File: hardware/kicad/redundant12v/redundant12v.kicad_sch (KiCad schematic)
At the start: 24 parts, among them J1 Conn_01x07, J2 IDC 2x5 Male, U1 ATTINY212-SSF, U2 TI MAX232EID, U3 LD1117S50CTR, X1 ECS-3951M-018-AU-TR

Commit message: Fix swapped anode and cathode labels
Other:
- note added: "(to anode of LEDs)"
- note added: "(to cathode)"
- note removed: "(to anode)"
- moved on the sheet: TP1, TP2, TP3
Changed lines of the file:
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@@
     (stroke (width 0) (type default) (color 0 0 0 0))
   )
-  (wire (pts (xy 255.27 41.91) (xy 259.08 41.91))
+  (wire (pts (xy 255.27 39.37) (xy 259.08 39.37))
     (stroke (width 0) (type default) (color 0 0 0 0))
   )
@@
     (stroke (width 0) (type default) (color 0 0 0 0))
   )
-  (wire (pts (xy 257.81 34.29) (xy 259.08 34.29))
+  (wire (pts (xy 257.81 31.75) (xy 259.08 31.75))
     (stroke (width 0) (type default) (color 0 0 0 0))
   )
@@
     (stroke (width 0) (type default) (color 0 0 0 0))
   )
-  (wire (pts (xy 257.81 33.02) (xy 257.81 34.29))
+  (wire (pts (xy 257.81 30.48) (xy 257.81 31.75))
     (stroke (width 0) (type default) (color 0 0 0 0))
   )
@@
     (stroke (width 0) (type default) (color 0 0 0 0))
   )
-  (wire (pts (xy 257.81 48.26) (xy 259.08 48.26))
+  (wire (pts (xy 257.81 45.72) (xy 259.08 45.72))
     (stroke (width 0) (type default) (color 0 0 0 0))
   )
@@
     (effects (font (size 1.27 1.27)) (justify left bottom))
   )
+  (text "(to anode\n  of LEDs)" (at 276.86 63.5 180)
+    (effects (font (size 1.27 1.27)) (justify right bottom))
+  )
   (text "DCD" (at 252.73 114.3 0)
     (effects (font (size 1.27 1.27)) (justify left bottom))
   )
-  (text "(to anode)" (at 73.66 93.98 180)
+  (text "(to cathode)" (at 76.2 93.98 180)
     (effects (font (size 1.27 1.27)) (justify right bottom))
   )
@@
     (effects (font (size 1.27 1.27)) (justify left bottom))
   )
-  (text "(to anode)" (at 71.12 124.46 180)
+  (text "(to cathode)" (at 71.12 124.46 180)
     (effects (font (size 1.27 1.27)) (justify right bottom))
   )
@@
     )
   )
-  (global_label "UPDI" (shape input) (at 255.27 41.91 180) (fields_autoplaced)
+  (global_label "UPDI" (shape input) (at 255.27 39.37 180) (fields_autoplaced)
     (effects (font (size 1.27 1.27)) (justify right))
-    (property "Referenzen zwischen Schaltplänen" "${INTERSHEET_REFS}" (id 0) (at 248.3817 41.8306 0)
+    (property "Referenzen zwischen Schaltplänen" "${INTERSHEET_REFS}" (id 0) (at 248.3817 39.2906 0)
       (effects (font (size 1.27 1.27)) (justify right) hide)
     )
@@
     (pin "1")
   )
-  (symbol (lib_id "Connector:TestPoint") (at 259.08 34.29 270) (unit 1)
-    (in_bom yes) (on_board yes) (fields_autoplaced)
-    (property "Reference" "TP1" (id 0) (at 264.16 33.0199 90)
-      (effects (font (size 1.27 1.27)) (justify left))
-    )
-    (property "Value" "VTG_5V" (id 1) (at 264.16 35.5599 90)
-      (effects (font (size 1.27 1.27)) (justify left))
-    )
-    (property "Footprint" "TestPoint:TestPoint_Pad_D2.5mm" (id 2) (at 259.08 39.37 0)
-      (effects (font (size 1.27 1.27)) hide)
-    )
-    (property "Datasheet" "~" (id 3) (at 259.08 39.37 0)
+  (symbol (lib_id "Connector:TestPoint") (at 259.08 31.75 270) (unit 1)
+    (in_bom yes) (on_board yes) (fields_autoplaced)
+    (property "Reference" "TP1" (id 0) (at 264.16 30.4799 90)
+      (effects (font (size 1.27 1.27)) (justify left))
+    )
+    (property "Value" "VTG_5V" (id 1) (at 264.16 33.0199 90)
+      (effects (font (size 1.27 1.27)) (justify left))
+    )
+    (property "Footprint" "TestPoint:TestPoint_Pad_D2.5mm" (id 2) (at 259.08 36.83 0)
+      (effects (font (size 1.27 1.27)) hide)
+    )
+    (property "Datasheet" "~" (id 3) (at 259.08 36.83 0)
       (effects (font (size 1.27 1.27)) hide)
     )
@@
     (pin "2")
   )
-  (symbol (lib_id "Connector:TestPoint") (at 259.08 41.91 270) (unit 1)
-    (in_bom yes) (on_board yes) (fields_autoplaced)
-    (property "Reference" "TP2" (id 0) (at 264.16 40.6399 90)
-      (effects (font (size 1.27 1.27)) (justify left))
-    )
-    (property "Value" "UPDI" (id 1) (at 264.16 43.1799 90)
-      (effects (font (size 1.27 1.27)) (justify left))
-    )
-    (property "Footprint" "TestPoint:TestPoint_Pad_D2.5mm" (id 2) (at 259.08 46.99 0)
-      (effects (font (size 1.27 1.27)) hide)
-    )
-    (property "Datasheet" "~" (id 3) (at 259.08 46.99 0)
+  (symbol (lib_id "Connector:TestPoint") (at 259.08 39.37 270) (unit 1)
+    (in_bom yes) (on_board yes) (fields_autoplaced)
+    (property "Reference" "TP2" (id 0) (at 264.16 38.0999 90)
+      (effects (font (size 1.27 1.27)) (justify left))
+    )
+    (property "Value" "UPDI" (id 1) (at 264.16 40.6399 90)
+      (effects (font (size 1.27 1.27)) (justify left))
+    )
+    (property "Footprint" "TestPoint:TestPoint_Pad_D2.5mm" (id 2) (at 259.08 44.45 0)
+      (effects (font (size 1.27 1.27)) hide)
+    )
+    (property "Datasheet" "~" (id 3) (at 259.08 44.45 0)
       (effects (font (size 1.27 1.27)) hide)
     )
@@
     (pin "3")
   )
-  (symbol (lib_id "power:GND") (at 257.81 48.26 0) (unit 1)
-    (in_bom yes) (on_board yes) (fields_autoplaced)
-    (property "Reference" "#PWR0114" (id 0) (at 257.81 54.61 0)
-      (effects (font (size 1.27 1.27)) hide)
-    )
-    (property "Value" "GND" (id 1) (at 257.81 53.34 0))
-    (property "Footprint" "" (id 2) (at 257.81 48.26 0)
-      (effects (font (size 1.27 1.27)) hide)
-    )
-    (property "Datasheet" "" (id 3) (at 257.81 48.26 0)
+  (symbol (lib_id "power:GND") (at 257.81 45.72 0) (unit 1)
+    (in_bom yes) (on_board yes) (fields_autoplaced)
+    (property "Reference" "#PWR0114" (id 0) (at 257.81 52.07 0)
+      (effects (font (size 1.27 1.27)) hide)
+    )
+    (property "Value" "GND" (id 1) (at 257.81 50.8 0))
+    (property "Footprint" "" (id 2) (at 257.81 45.72 0)
+      (effects (font (size 1.27 1.27)) hide)
+    )
+    (property "Datasheet" "" (id 3) (at 257.81 45.72 0)
       (effects (font (size 1.27 1.27)) hide)
     )
@@
     (pin "1")
   )
-  (symbol (lib_id "power:VCC") (at 257.81 33.02 0) (unit 1)
-    (in_bom yes) (on_board yes) (fields_autoplaced)
-    (property "Reference" "#PWR0116" (id 0) (at 257.81 36.83 0)
-      (effects (font (size 1.27 1.27)) hide)
-    )
-    (property "Value" "VCC" (id 1) (at 257.81 27.94 0))
-    (property "Footprint" "" (id 2) (at 257.81 33.02 0)
-      (effects (font (size 1.27 1.27)) hide)
-    )
-    (property "Datasheet" "" (id 3) (at 257.81 33.02 0)
+  (symbol (lib_id "power:VCC") (at 257.81 30.48 0) (unit 1)
+    (in_bom yes) (on_board yes) (fields_autoplaced)
+    (property "Reference" "#PWR0116" (id 0) (at 257.81 34.29 0)
+      (effects (font (size 1.27 1.27)) hide)
+    )
+    (property "Value" "VCC" (id 1) (at 257.81 25.4 0))
+    (property "Footprint" "" (id 2) (at 257.81 30.48 0)
+      (effects (font (size 1.27 1.27)) hide)
+    )
+    (property "Datasheet" "" (id 3) (at 257.81 30.48 0)
       (effects (font (size 1.27 1.27)) hide)
     )
@@
     (pin "3")
   )
-  (symbol (lib_id "Connector:TestPoint") (at 259.08 48.26 270) (unit 1)
-    (in_bom yes) (on_board yes) (fields_autoplaced)
-    (property "Reference" "TP3" (id 0) (at 264.16 46.9899 90)
-      (effects (font (size 1.27 1.27)) (justify left))
-    )
-    (property "Value" "GND" (id 1) (at 264.16 49.5299 90)
-      (effects (font (size 1.27 1.27)) (justify left))
-    )
-    (property "Footprint" "TestPoint:TestPoint_Pad_D2.5mm" (id 2) (at 259.08 53.34 0)
-      (effects (font (size 1.27 1.27)) hide)
-    )
-    (property "Datasheet" "~" (id 3) (at 259.08 53.34 0)
-      (effects (font (size 1.27 1.27)) hide)
-    )
+  (symbol (lib_id "Connector:TestPoint") (at 259.08 45.72 270) (unit 1)
+    (in_bom yes) (on_board yes) (fields_autoplaced)
+    (property "Reference" "TP3" (id 0) (at 264.16 44.4499 90)
+      (effects (font (size 1.27 1.27)) (justify left))
+    )
+    (property "Value" "GND" (id 1) (at 264.16 46.9899 90)
+      (effects (font (size 1.27 1.27)) (justify left))
+    )
+    (property "Footprint" "TestPoint:TestPoint_Pad_D2.5mm" (id 2) (at 259.08 50.8 0)
+      (effects (font (size 1.27 1.27)) hide)
+    )
+    (property "Datasheet" "~" (id 3) (at 259.08 50.8 0)
+      (effects (font (size 1.27 1.27)) hide)
+    )

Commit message: Resistors R1, R2 are now 47K
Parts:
- R1, R2: value 10K -> 47K
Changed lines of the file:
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@@
     (in_bom yes) (on_board yes)
     (property "Reference" "R2" (id 0) (at 46.99 115.57 90))
-    (property "Value" "10K" (id 1) (at 46.99 110.49 90))
+    (property "Value" "47K" (id 1) (at 46.99 110.49 90))
     (property "Footprint" "Resistor_SMD:R_0805_2012Metric_Pad1.20x1.40mm_HandSolder" (id 2) (at 44.45 113.03 0)
       (effects (font (size 1.27 1.27)) hide)
@@
       (effects (font (size 1.27 1.27)) (justify left))
     )
-    (property "Value" "10K" (id 1) (at 46.99 82.55 90)
+    (property "Value" "47K" (id 1) (at 46.99 82.55 90)
       (effects (font (size 1.27 1.27)) (justify left))
     )
@@
     )
     (path "/da76e409-da8b-42c9-938b-4b030245eb99"
-      (reference "R1") (unit 1) (value "10K") (footprint "Resistor_SMD:R_0805_2012Metric_Pad1.20x1.40mm_HandSolder")
+      (reference "R1") (unit 1) (value "47K") (footprint "Resistor_SMD:R_0805_2012Metric_Pad1.20x1.40mm_HandSolder")
     )
     (path "/ce21a548-d04b-4c0a-9ef4-b913d9d19def"
-      (reference "R2") (unit 1) (value "10K") (footprint "Resistor_SMD:R_0805_2012Metric_Pad1.20x1.40mm_HandSolder")
+      (reference "R2") (unit 1) (value "47K") (footprint "Resistor_SMD:R_0805_2012Metric_Pad1.20x1.40mm_HandSolder")
     )
     (path "/de0a58e5-7f3d-4ccf-ac8a-4cd50321ae36"

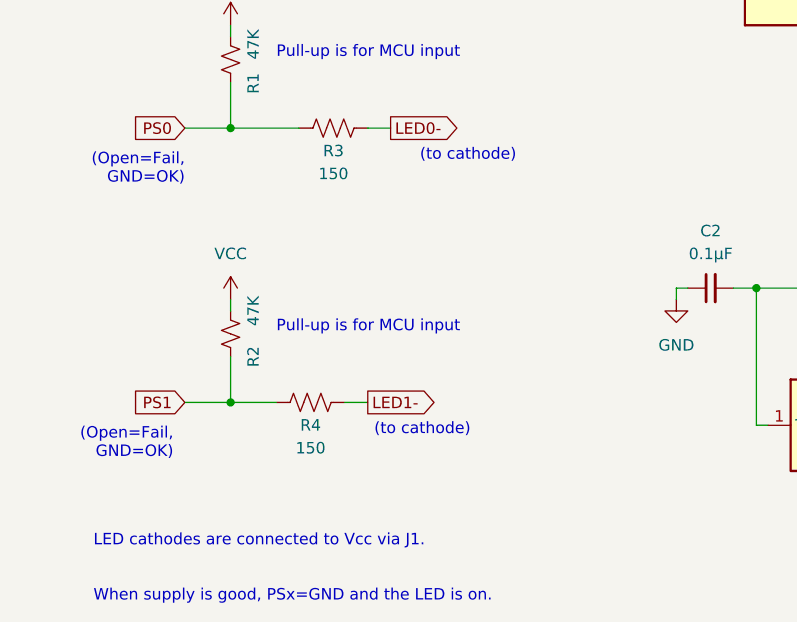
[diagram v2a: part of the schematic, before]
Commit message: Fix values of R3 and R4 on schematic
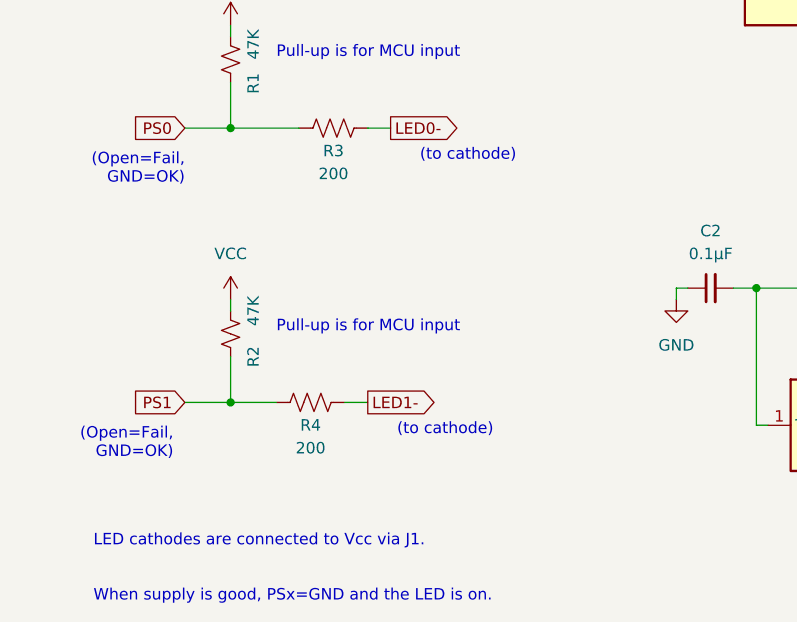
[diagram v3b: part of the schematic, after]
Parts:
- R3, R4: value 150 -> 200
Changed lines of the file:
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@@
     (effects (font (size 1.27 1.27)) (justify left bottom))
   )
-  (text "(to cathode)" (at 71.12 124.46 180)
+  (text "(to cathode)" (at 73.66 124.46 180)
     (effects (font (size 1.27 1.27)) (justify right bottom))
   )
@@
     (in_bom yes) (on_board yes)
     (property "Reference" "R4" (id 0) (at 53.34 123.19 90))
-    (property "Value" "150" (id 1) (at 53.34 125.73 90))
+    (property "Value" "200" (id 1) (at 53.34 125.73 90))
     (property "Footprint" "Resistor_SMD:R_0805_2012Metric_Pad1.20x1.40mm_HandSolder" (id 2) (at 53.594 119.634 90)
       (effects (font (size 1.27 1.27)) hide)
@@
     (in_bom yes) (on_board yes)
     (property "Reference" "R3" (id 0) (at 55.88 92.71 90))
-    (property "Value" "150" (id 1) (at 55.88 95.25 90))
+    (property "Value" "200" (id 1) (at 55.88 95.25 90))
     (property "Footprint" "Resistor_SMD:R_0805_2012Metric_Pad1.20x1.40mm_HandSolder" (id 2) (at 56.134 89.154 90)
       (effects (font (size 1.27 1.27)) hide)
@@
     )
     (path "/de0a58e5-7f3d-4ccf-ac8a-4cd50321ae36"
-      (reference "R3") (unit 1) (value "150") (footprint "Resistor_SMD:R_0805_2012Metric_Pad1.20x1.40mm_HandSolder")
+      (reference "R3") (unit 1) (value "200") (footprint "Resistor_SMD:R_0805_2012Metric_Pad1.20x1.40mm_HandSolder")
     )
     (path "/536d55a4-3759-4f62-a47d-eabc58b4f4c3"
-      (reference "R4") (unit 1) (value "150") (footprint "Resistor_SMD:R_0805_2012Metric_Pad1.20x1.40mm_HandSolder")
+      (reference "R4") (unit 1) (value "200") (footprint "Resistor_SMD:R_0805_2012Metric_Pad1.20x1.40mm_HandSolder")
     )
     (path "/27cb06f6-9b54-4054-b209-1cfd8823978c"
